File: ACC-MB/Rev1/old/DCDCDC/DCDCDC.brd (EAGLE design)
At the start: 89.8 x 62 mm, 21 parts, among them X2 5566-4

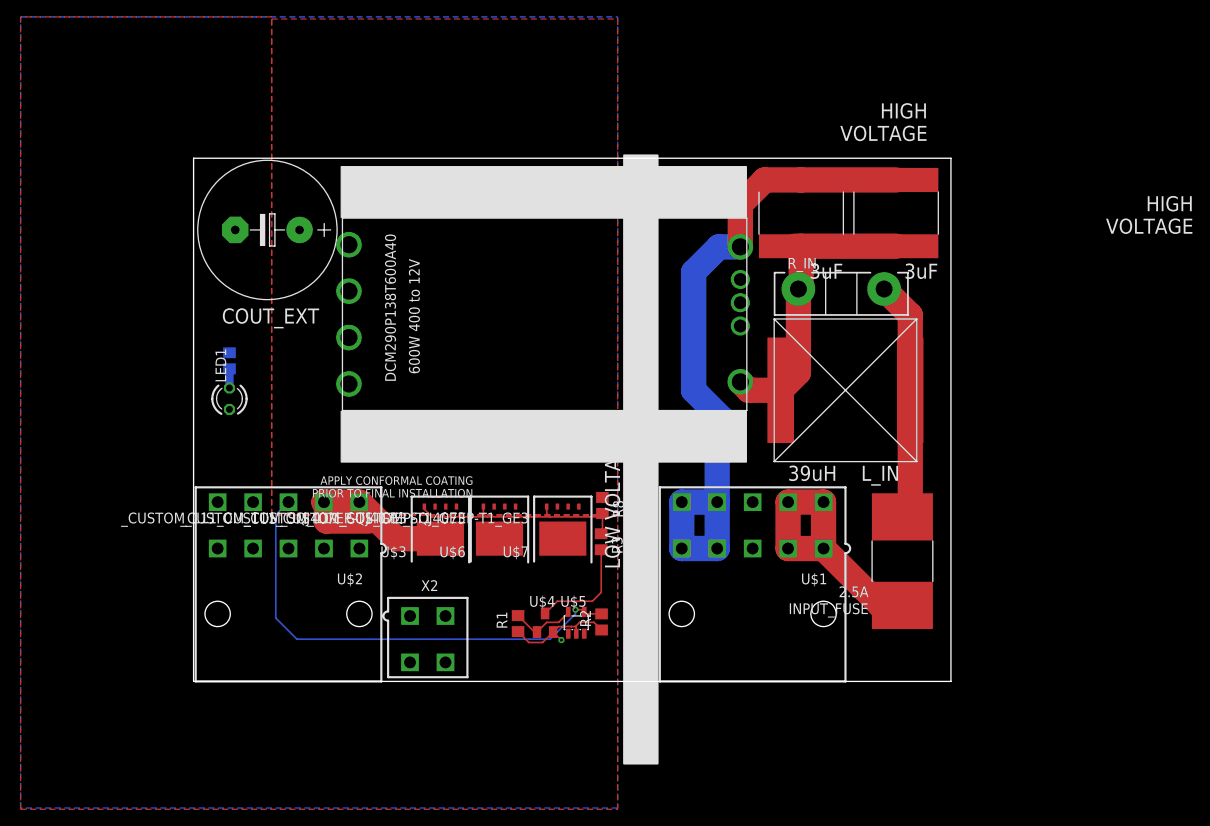
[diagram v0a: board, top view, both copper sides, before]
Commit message: 7792 added to all DC
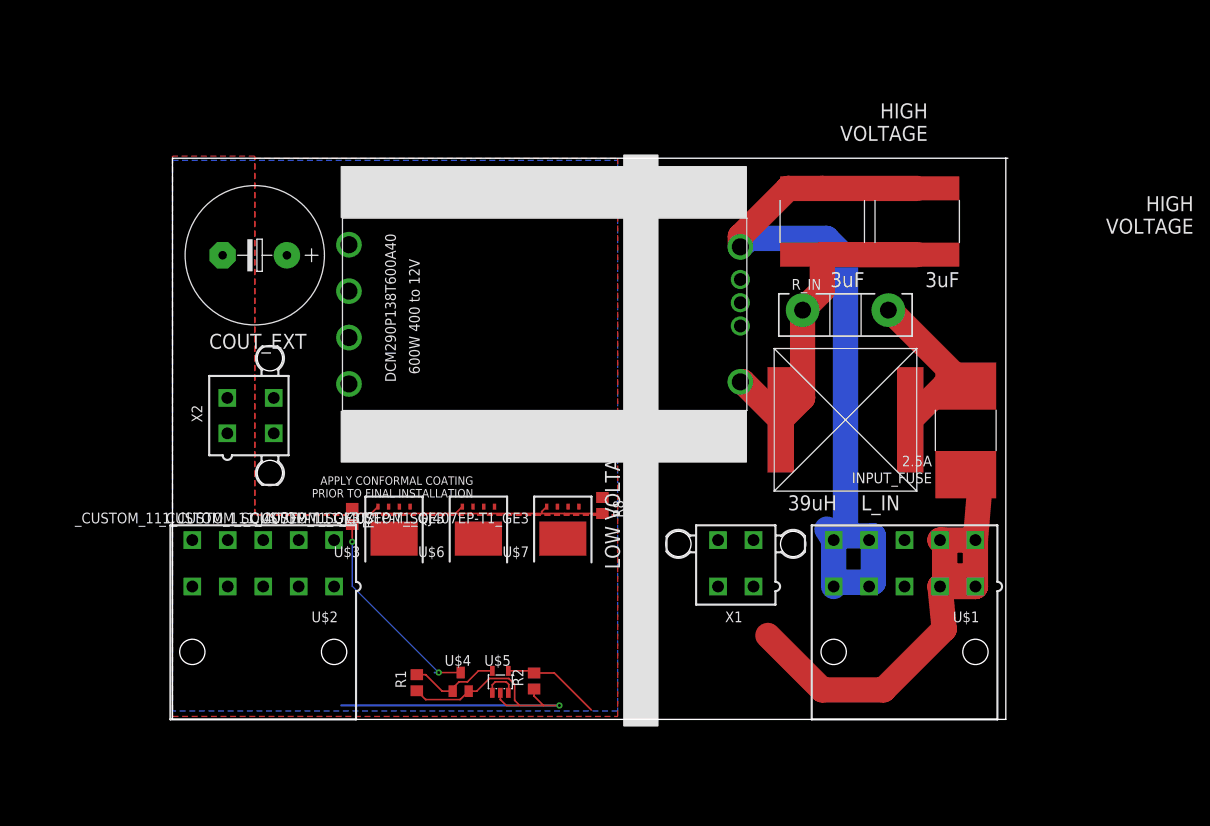
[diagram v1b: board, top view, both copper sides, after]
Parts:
- removed LED1: (no value), ACC-MB-R0:LED3MM
- removed R4: (no value), ACC-MB-R0:R0805
- added X1: 5566-4, ACC-MB-R0:5566-4
- moved X2 33.8 mm to (9.50, 36.0), turned to 270 degrees
- moved R3 29.7 mm to (21.6, 24.1)
- moved U$1 18.6 mm to (87.0, 18.5)
- moved INPUT_FUSE 17.2 mm to (94.2, 34.2)
- moved R1 13.9 mm to (29.2, 4.35)
- moved U$4 12.2 mm to (34.4, 4.45)
- moved U$5 11.4 mm to (39.1, 4.45)
- moved R2 10.6 mm to (43.1, 4.55)
- moved U$3 5.50 mm to (26.5, 22.5)
- moved U$2 5.41 mm to (11.0, 18.5)
- moved L_IN 3.50 mm to (80.0, 35.5)
- moved COUT_EXT 3.35 mm to (10.0, 55.0)
- moved CFILTER_1 2.69 mm to (88.5, 59.0)
- moved CFILTER_2 2.69 mm to (77.2, 59.0)
- moved R_IN 2.55 mm to (80.0, 48.5)
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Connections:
- removed net N$5: LED1.K, R4.2
- net +12V: now also U$2.4, U$2.5; no longer LED1.A, U$2.6, U$2.7
- net GND: now also U$2.6, U$2.7; no longer R4.1, U$2.3, U$2.4, U$2.5
- net V+: now also X1.1, X1.2
- net V-: now also X1.3, X1.4
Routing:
- net PRECH_ACTIVE: track 56.0 -> 11.7 mm, vias 1 -> 0
- net GND: track 14.1 -> 52.5 mm
- net V+: track 31.5 -> 63.1 mm
- net +12V: track 23.0 -> 4.19 mm
- net V-: track 81.6 -> 95.9 mm
- net N$4: track 12.7 -> 24.9 mm, vias 0 -> 2
- net V+_FUSED: track 28.7 -> 21.1 mm
- net N$1: track 27.2 -> 33.5 mm
- net N$3: track 38.4 -> 42.6 mm
- net N$2: track 7.81 -> 11.0 mm
- net N$5: track 2.28 -> 0.00 mm
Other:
- board size 89.8 x 62 mm -> 99 x 66.5 mm
